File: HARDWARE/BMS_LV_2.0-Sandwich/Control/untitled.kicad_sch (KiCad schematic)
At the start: 19 parts, among them J3 FTSH-107-01-L-D-K, U1 STM32G484RETx, Y1 ATX-11-F-32.000MHZ-F05-T

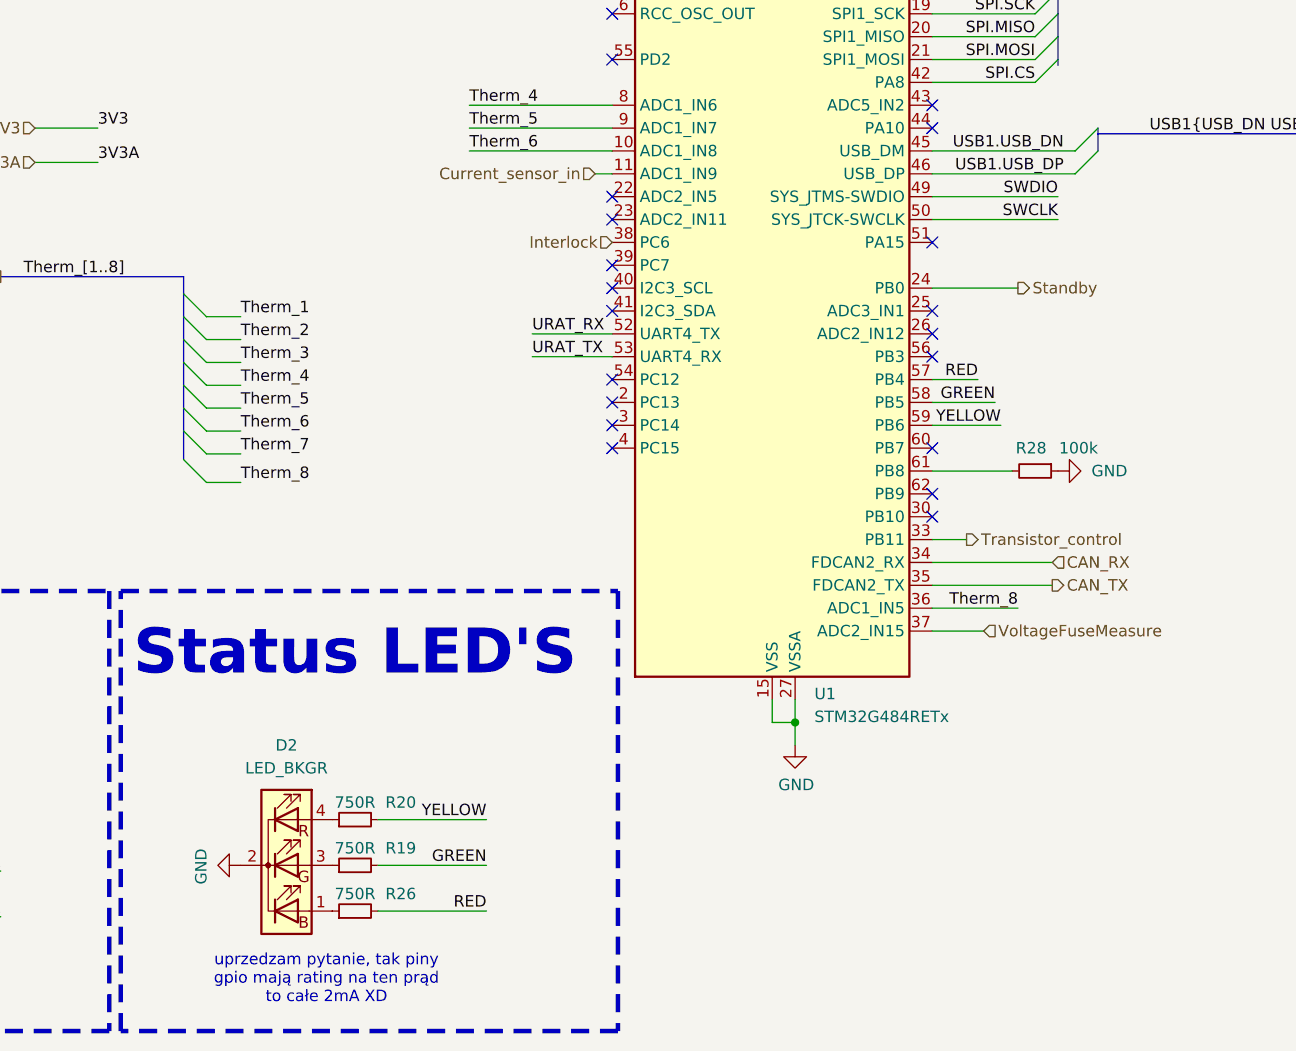
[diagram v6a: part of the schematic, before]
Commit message: Zmieniono ledy, przesunięto pomiar napięcia z czujnika prądu na adc2
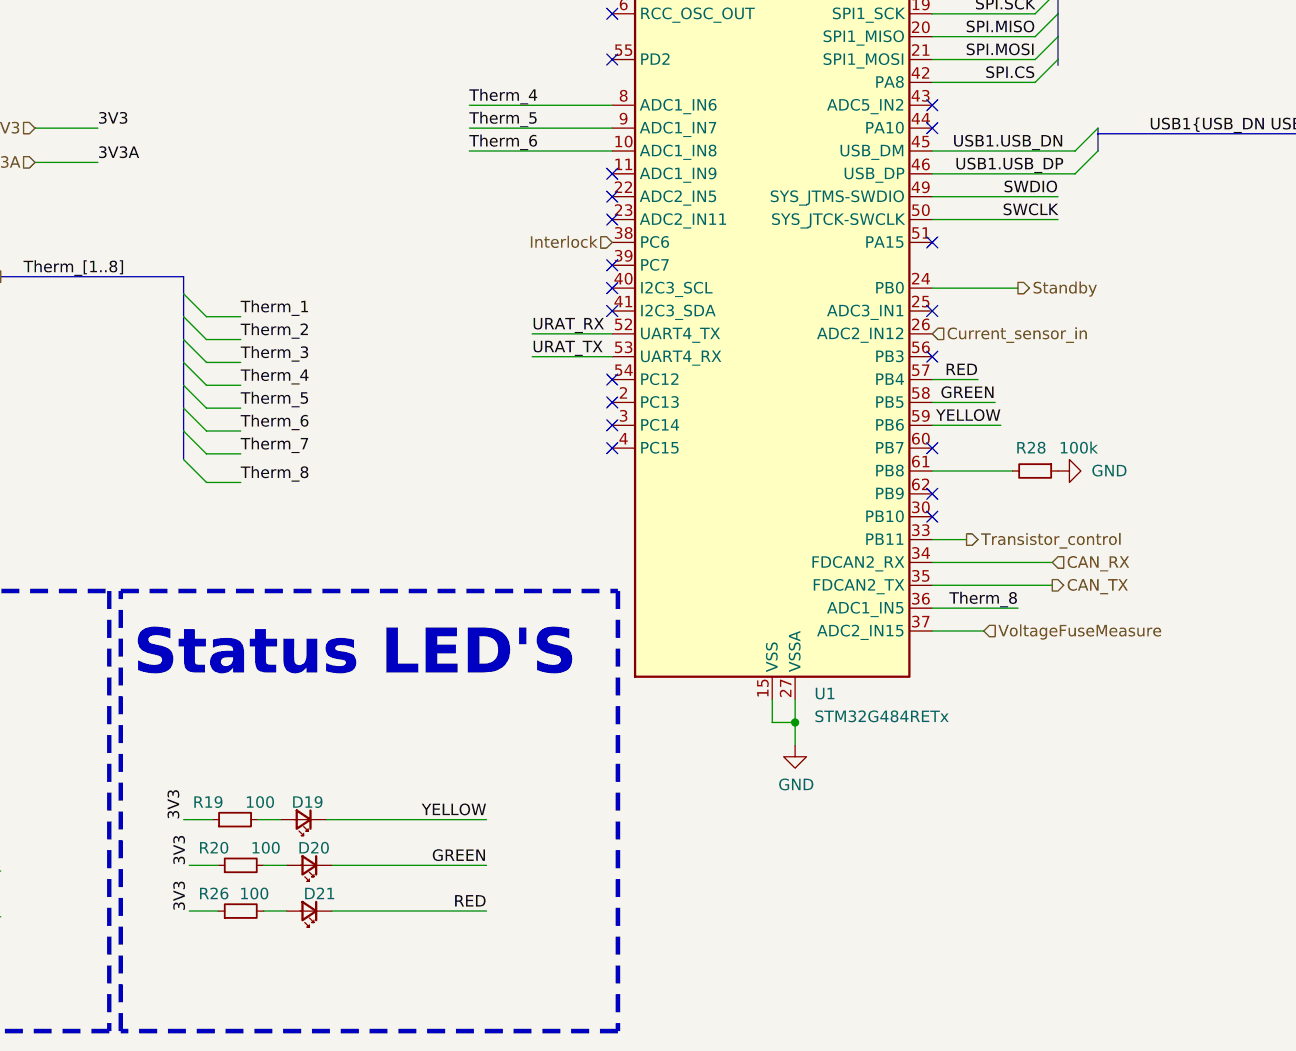
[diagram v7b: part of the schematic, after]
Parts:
- removed D2: LED_BKGR, Footprint:APFA2507LSURKSYKZGKC, symbol Device:LED_BKGR
- added D19, D20, D21: (no value), LED_SMD:LED_0603_1608Metric_Pad1.05x0.95mm_HandSolder, symbol Device:LED_Small
- R19, R20, R26: value 750R -> 100; Mouser Price/Stock (none) -> https://www.mouser.pl/ProductDetail/Vishay-Dale/CRCW06031K0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
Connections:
- net 3V3: now also R19.1, R20.1, R26.1
- net Current_sensor_in: now also U1.26 (PB2); no longer U1.11 (PC3)
- net GREEN: now also D20.1 (K); no longer R19.2
- net RED: now also D21.1 (K); no longer R26.2
- net YELLOW: now also D19.1 (K); no longer R20.2
- new net: D21.2 (A), R26.2
- new net: D19.2 (A), R19.2
- new net: D20.2 (A), R20.2
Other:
- note removed: "uprzedzam pytanie, tak piny gpio mają rating na ten prąd to całe 2mA XD"

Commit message: Poprawki , tvs , programator
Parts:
- D7, D8: footprint SOT95P285X140-6N -> Footprint:SOT65P210X110-6N; Mouser Part Number 621-D5V0P4UR6SO-7 -> D1213A-04S-7
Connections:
- net 3V3: now also D7.5 (VCC), D8.5 (VCC)
- net GND: no longer D7.5 (VCC), D8.5 (VCC)
- net URAT_RX: now also D8.6 (I/O4); no longer D8.4 (I/O3)
- net URAT_TX: now also D8.4 (I/O3); no longer D8.6 (I/O4)
